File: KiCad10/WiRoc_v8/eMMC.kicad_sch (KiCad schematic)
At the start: 10 parts, among them U14 KLM8G1GETF-B041

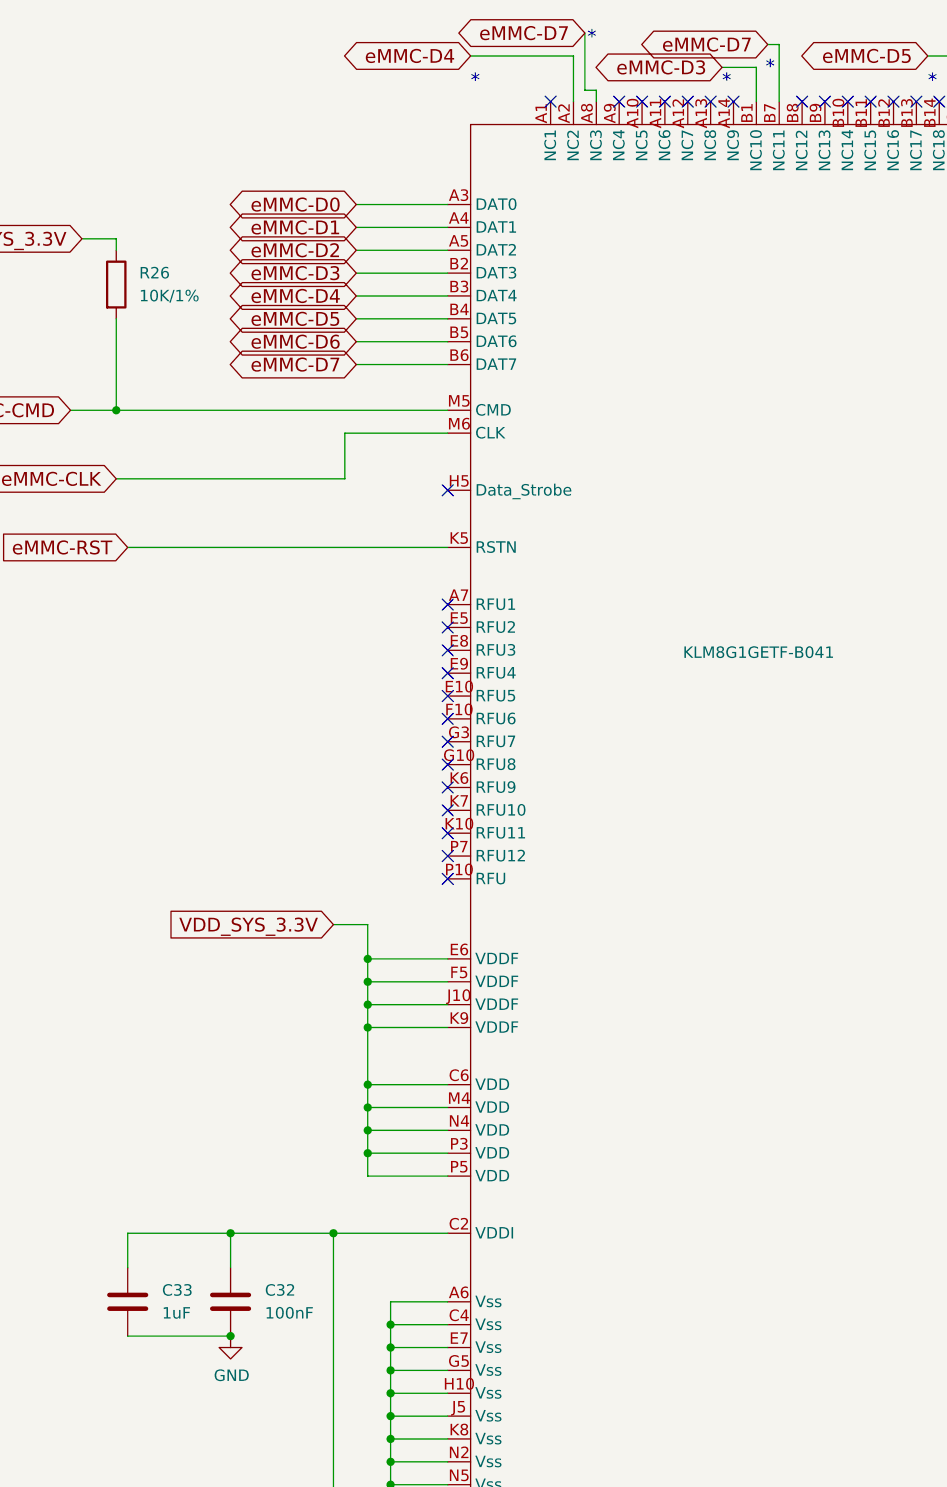
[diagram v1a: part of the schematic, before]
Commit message: add logo, improve layout
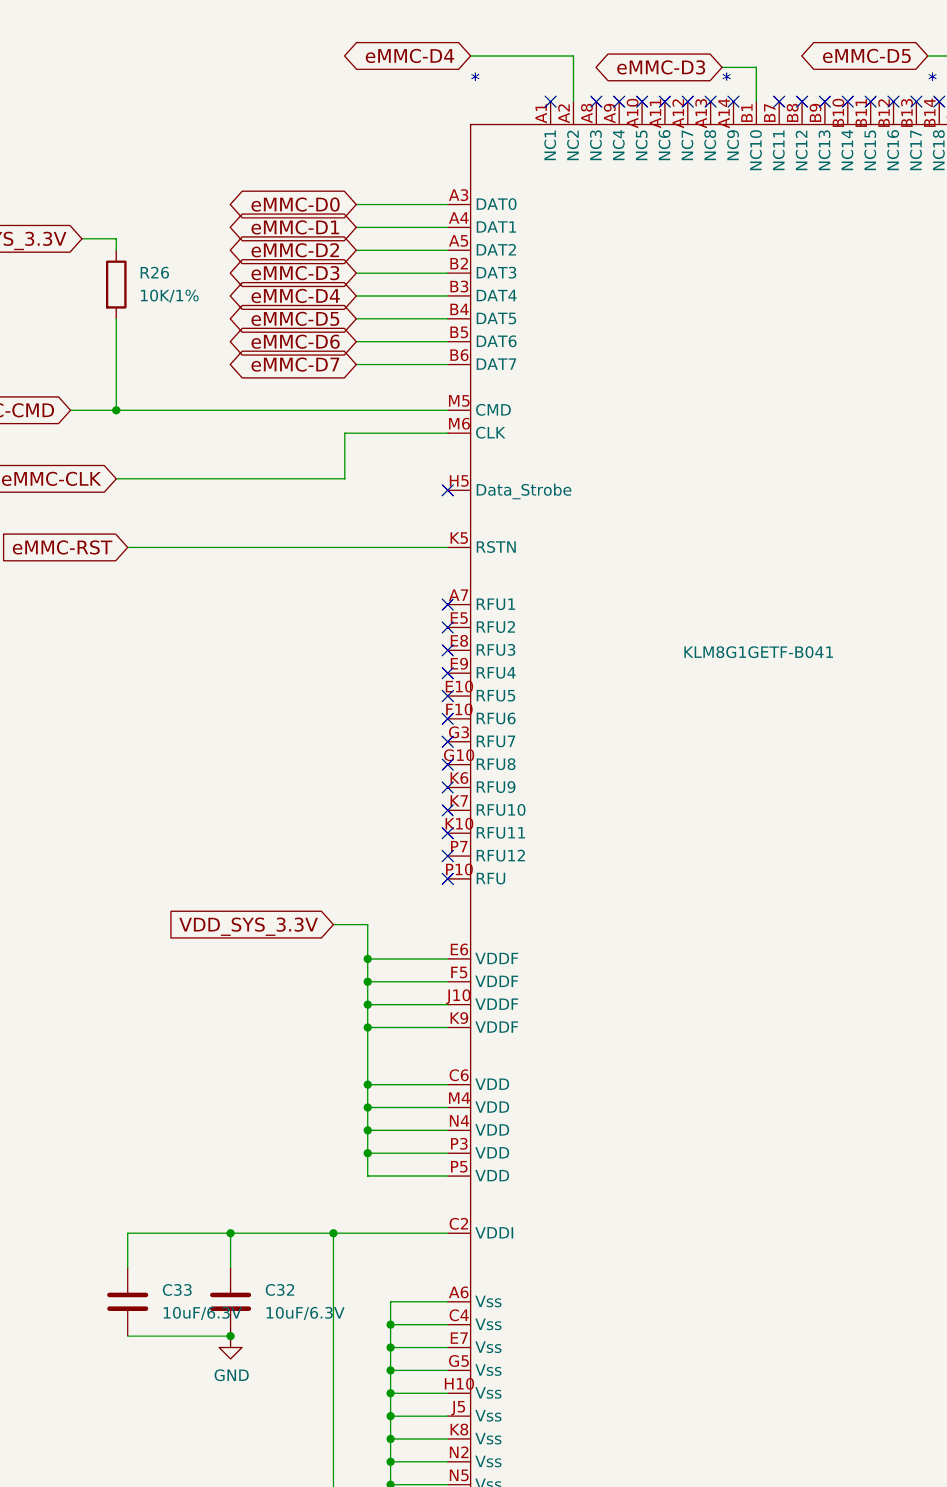
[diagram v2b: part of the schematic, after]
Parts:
- C32: value 100nF -> 10uF/6.3V; LCSC Part # C1525 -> C15525; ManufacturerPartNumber CL05B104KO5NNNC -> CL05A106MQ5NUNC
- C33: value 1uF -> 10uF/6.3V; LCSC Part # C52923 -> C15525; ManufacturerPartNumber CL05A105KA5NQNC -> CL05A106MQ5NUNC
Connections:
- net eMMC-D7: no longer U14.A8 (NC3), U14.B7 (NC11)
- no-connect marks 109 -> 111
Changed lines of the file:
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@@
 (kicad_sch
-	(version 20260326)
+	(version 20260306)
 	(generator "eeschema")
-	(generator_version "10.99")
+	(generator_version "10.0")
 	(paper "A4")
 	(text "*"
@@
 	(text "*"
 		(exclude_from_sim no)
-		(at 107.696 17.526 0)
-		(effects
-			(font
-				(size 1.524 1.524)
-			)
-			(justify left bottom)
-		)
-	)
-	(text "*"
-		(exclude_from_sim no)
 		(at 125.73 19.05 0)
 		(effects
@@
 	(text "*"
 		(exclude_from_sim no)
-		(at 87.884 14.224 0)
-		(effects
-			(font
-				(size 1.524 1.524)
-			)
-			(justify left bottom)
-		)
-	)
-	(text "*"
-		(exclude_from_sim no)
 		(at 100.33 193.04 0)
 		(effects
@@
 	)
 	(no_connect
+		(at 109.22 20.32)
+	)
+	(no_connect
 		(at 160.02 152.4)
 	)
@@
 	)
 	(no_connect
+		(at 88.9 20.32)
+	)
+	(no_connect
 		(at 137.16 189.23)
 	)
@@
 	(wire
 		(pts
-			(xy 107.95 13.97) (xy 109.22 13.97)
-		)
-		(stroke
-			(width 0)
-			(type default)
-		)
-	)
-	(wire
-		(pts
 			(xy 31.75 35.56) (xy 35.56 35.56)
 		)
@@
 	(wire
 		(pts
-			(xy 109.22 13.97) (xy 109.22 20.32)
-		)
-		(stroke
-			(width 0)
-			(type default)
-		)
-	)
-	(wire
-		(pts
 			(xy 63.5 120.65) (xy 63.5 118.11)
 		)
@@
 	(wire
 		(pts
-			(xy 88.9 19.05) (xy 88.9 20.32)
-		)
-		(stroke
-			(width 0)
-			(type default)
-		)
-	)
-	(wire
-		(pts
 			(xy 63.5 118.11) (xy 72.39 118.11)
 		)
@@
 	(wire
 		(pts
-			(xy 87.63 12.7) (xy 87.63 19.05)
-		)
-		(stroke
-			(width 0)
-			(type default)
-		)
-	)
-	(wire
-		(pts
-			(xy 87.63 19.05) (xy 88.9 19.05)
-		)
-		(stroke
-			(width 0)
-			(type default)
-		)
-	)
-	(wire
-		(pts
 			(xy 66.04 163.83) (xy 66.04 166.37)
 		)
@@
 		)
 	)
-	(global_label "eMMC-D7"
-		(shape bidirectional)
-		(at 107.95 13.97 180)
-		(fields_autoplaced yes)
-		(effects
-			(font
-				(size 1.524 1.524)
-			)
-			(justify right)
-		)
-		(property "Intersheetrefs" "${INTERSHEET_REFS}"
-			(at 92.8342 13.97 0)
-			(hide yes)
-			(show_name no)
-			(do_not_autoplace no)
-			(effects
-				(font
-					(size 1.27 1.27)
-				)
-				(justify right)
-			)
-		)
-	)
 	(global_label "eMMC-D4"
 		(shape bidirectional)
@@
 		)
 	)
-	(global_label "eMMC-D7"
-		(shape bidirectional)
-		(at 87.63 12.7 180)
-		(fields_autoplaced yes)
-		(effects
-			(font
-				(size 1.524 1.524)
-			)
-			(justify right)
-		)
-		(property "Intersheetrefs" "${INTERSHEET_REFS}"
-			(at 72.5142 12.7 0)
-			(hide yes)
-			(show_name no)
-			(do_not_autoplace no)
-			(effects
-				(font
-					(size 1.27 1.27)
-				)
-				(justify right)
-			)
-		)
-	)
 	(global_label "VDD_SYS_3.3V"
 		(shape input)
@@
 		(fields_autoplaced yes)
 		(property "Reference" "C32"
-			(at 52.07 152.4 0)
+			(at 52.07 152.3999 0)
 			(show_name no)
 			(do_not_autoplace no)
@@
 			)
 		)
-		(property "Value" "100nF"
-			(at 52.07 154.94 0)
+		(property "Value" "10uF/6.3V"
+			(at 52.07 154.9399 0)
 			(show_name no)
 			(do_not_autoplace no)
@@
 			)
 		)
-		(property "LCSC Part #" "C1525"
+		(property "LCSC Part #" "C15525"
 			(at 48.26 153.67 0)
 			(hide yes)
@@
 			)
 		)
-		(property "ManufacturerPartNumber" "CL05B104KO5NNNC"
+		(property "ManufacturerPartNumber" "CL05A106MQ5NUNC"
 			(at 48.26 153.67 0)
 			(hide yes)
@@
 		(fields_autoplaced yes)
 		(property "Reference" "C33"
-			(at 40.64 152.4 0)
+			(at 40.64 152.3999 0)
 			(show_name no)
 			(do_not_autoplace no)
@@
 			)
 		)
-		(property "Value" "1uF"
-			(at 40.64 154.94 0)
+		(property "Value" "10uF/6.3V"
+			(at 40.64 154.9399 0)
 			(show_name no)
 			(do_not_autoplace no)
@@
 			)
 		)
-		(property "LCSC Part #" "C52923"
+		(property "LCSC Part #" "C15525"
 			(at 36.83 153.67 0)
 			(hide yes)
@@
 			)
 		)
-		(property "ManufacturerPartNumber" "CL05A105KA5NQNC"
+		(property "ManufacturerPartNumber" "CL05A106MQ5NUNC"
 			(at 36.83 153.67 0)
 			(hide yes)
